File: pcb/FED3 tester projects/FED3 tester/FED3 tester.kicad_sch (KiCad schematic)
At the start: 33 parts, among them J1 USB4105-GF-A, U1 FT232RL, U2 LP5907MFX-3.3, U3 LP5907MFX-3.3, U4 TPS79301DBVRG4

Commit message: FED3 tester - sync of the week
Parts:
- removed C14: 15pF, Capacitor_SMD:C_0603_1608Metric, symbol Device:C_Small
- removed C17: 10nF, Capacitor_SMD:C_0402_1005Metric, symbol Device:C_Small
- C15: value 4.7uF -> 10uF; footprint Capacitor_SMD:C_0603_1608Metric -> Capacitor_SMD:C_1206_3216Metric; MPN C1608X6S1C475K080AC -> GRM31CR71E106KA12L; OEPSPN OEPS010018 -> OEPS010007; TempCo X6S -> X5R; Voltage 16V -> 25V
- R7: value 61.2k -> 8k2; MPN RN73R1ETTP6122B25 -> ??; OEPSPN OEPS020214 -> ??
- R8: value 30.1k -> 4k; footprint Resistor_SMD:R_0603_1608Metric -> Resistor_SMD:R_0402_1005Metric; MPN RC0603FR-0730K1L -> ??; OEPSPN OEPS020132 -> ??
- U4: value TPS79301DBVRG4 -> TPS73801DCQR; footprint Package_TO_SOT_SMD:SOT-23-6 -> Package_TO_SOT_SMD:SOT-223-6; MPN TPS79301DBVRG4 -> TPS73801DCQR
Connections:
- net 3.7V: now also U4.2 (OUT); no longer U4.6 (OUT)
- net GND: now also U4.3 (GND), U4.6 (GND); no longer U4.2 (GND)
- net USB+5V: now also U4.5 (EN); no longer U4.3 (EN)
- net at U4.4 (FB): now also R7.1, R8.2
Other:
- moved on the sheet: C15, U4

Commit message: FED3 tester rev.B & FED3 tester support rev.B
-rev.B para 1ª revisão do Filipe
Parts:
- renumbered C15 to C14, C16 to C15
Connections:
- net at C4.1, C5.2, R6.2: now also J1.SH (SHIELD); no longer J1.S1 (SHIELD)
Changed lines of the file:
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@@
 		(dnp no)
 		(fields_autoplaced yes)
-		(property "Reference" "C15"
+		(property "Reference" "C14"
 			(at 97.79 158.7562 0)
 			(show_name no)
@@
 			(project "FED3 tester"
 				(path "/2ba63f12-2fcd-4471-9636-2762cde37de8"
-					(reference "C15")
+					(reference "C14")
 					(unit 1)
 				)
@@
 		(pin "B9"
 		)
-		(pin "S1"
+		(pin "SH"
 		)
 		(instances
@@
 		(in_pos_files yes)
 		(dnp no)
-		(property "Reference" "C16"
+		(property "Reference" "C15"
 			(at 57.15 167.6462 0)
 			(show_name no)
@@
 			(project "FED3 tester"
 				(path "/2ba63f12-2fcd-4471-9636-2762cde37de8"
-					(reference "C16")
+					(reference "C15")
 					(unit 1)
 				)

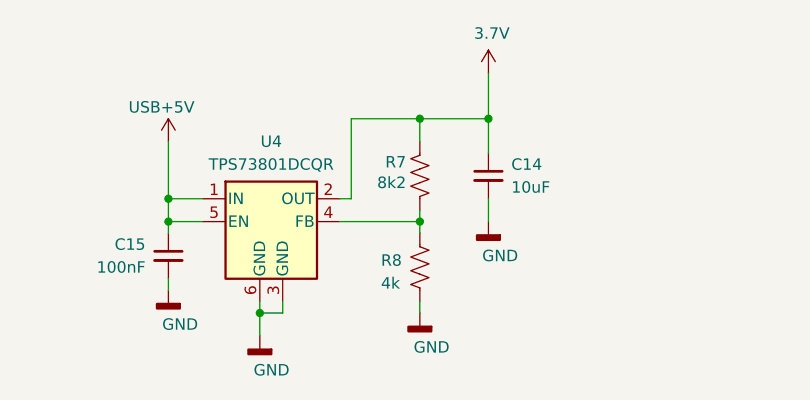
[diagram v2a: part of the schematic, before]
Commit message: completos OEPSPN & MPN
- andar de I-measure  ZXCT1086 redimensionado
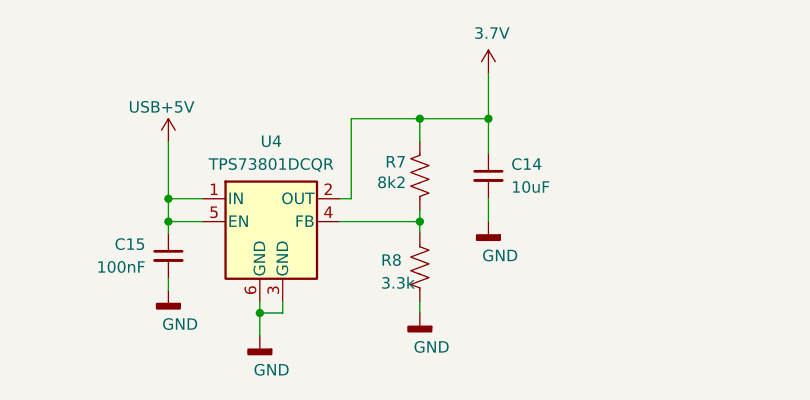
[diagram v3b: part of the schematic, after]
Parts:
- R7: footprint Resistor_SMD:R_0402_1005Metric -> Resistor_SMD:R_0603_1608Metric; MPN ?? -> ERJ-3EKF8201V; OEPSPN ?? -> OEPS020103; Tolerance 0.1% -> 1%
- R8: value 4k -> 3.3k; MPN ?? -> P3.30KLDKR-ND; OEPSPN ?? -> OEPS020083
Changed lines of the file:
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@@
 			)
 		)
-		(property "Footprint" "Resistor_SMD:R_0402_1005Metric"
+		(property "Footprint" "Resistor_SMD:R_0603_1608Metric"
 			(at 88.646 159.766 90)
 			(hide yes)
@@
 			)
 		)
-		(property "MPN" "??"
+		(property "MPN" "ERJ-3EKF8201V"
 			(at 78.867 163.068 0)
 			(hide yes)
@@
 			)
 		)
-		(property "OEPSPN" "??"
+		(property "OEPSPN" "OEPS020103"
 			(at 87.63 160.02 0)
 			(hide yes)
@@
 			)
 		)
-		(property "Tolerance" "0.1%"
+		(property "Tolerance" "1%"
 			(at 87.63 160.02 0)
 			(hide yes)
@@
 			)
 		)
-		(property "Value" "4k"
+		(property "Value" "3.3k"
 			(at 83.312 171.958 0)
 			(show_name no)
@@
 			)
 		)
-		(property "MPN" "??"
+		(property "MPN" "P3.30KLDKR-ND"
 			(at 96.393 173.228 0)
 			(hide yes)
@@
 			)
 		)
-		(property "OEPSPN" "??"
+		(property "OEPSPN" "OEPS020083"
 			(at 87.63 170.18 0)
 			(hide yes)

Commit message: revistos OEPSPN & MPN com gsheet - OK
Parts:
- R8: MPN P3.30KLDKR-ND -> ERJ-2RKF3301X
- U4: OEPSPN OEPS080129 -> OEPS080085
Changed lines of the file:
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@@
 			)
 		)
-		(property "OEPSPN" "OEPS080129"
+		(property "OEPSPN" "OEPS080085"
 			(at 70.866 174.752 0)
 			(hide yes)
@@
 			)
 		)
-		(property "Description" ""
+		(property "Description" "SMD 0603 8.2kΩ ±1% 0.100W"
 			(at 87.63 160.02 0)
 			(hide yes)
@@
 			)
 		)
-		(property "Description" ""
+		(property "Description" "SMD 0402 2kΩ ±1% 0.100W"
 			(at 87.63 170.18 0)
 			(hide yes)
@@
 			)
 		)
-		(property "MPN" "P3.30KLDKR-ND"
+		(property "MPN" "ERJ-2RKF3301X"
 			(at 96.393 173.228 0)
 			(hide yes)
